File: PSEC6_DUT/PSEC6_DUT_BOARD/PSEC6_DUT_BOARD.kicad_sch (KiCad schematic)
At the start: 0 parts

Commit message: Added Additional Pages for Schematic Distribution
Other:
- added sheet ADC_Buffers (ADC_Buffers.kicad_sch)
- added sheet PLL (PLL.kicad_sch)
- added sheet PSEC6_Device (PSEC6_Device.kicad_sch)
- added sheet SAMTEC (SAMTEC.kicad_sch)
- added sheet SMA (SMA.kicad_sch)
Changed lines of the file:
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@@
 (kicad_sch
-	(version 20250114)
+	(version 20260306)
 	(generator "eeschema")
-	(generator_version "9.0")
-	(paper "A4")
+	(generator_version "10.0")
+	(paper "A3")
+	(sheet
+		(at 25.4 101.6)
+		(size 76.2 50.8)
+		(exclude_from_sim no)
+		(in_bom yes)
+		(on_board yes)
+		(dnp no)
+		(fields_autoplaced yes)
+		(stroke
+			(width 0.1524)
+			(type solid)
+		)
+		(fill
+			(color 0 0 0 0)
+		)
+		(property "Sheetname" "ADC_Buffers"
+			(at 25.4 100.8884 0)
+			(show_name no)
+			(do_not_autoplace no)
+			(effects
+				(font
+					(size 1.27 1.27)
+				)
+				(justify left bottom)
+			)
+		)
+		(property "Sheetfile" "ADC_Buffers.kicad_sch"
+			(at 25.4 152.9846 0)
+			(show_name no)
+			(do_not_autoplace no)
+			(effects
+				(font
+					(size 1.27 1.27)
+				)
+				(justify left top)
+			)
+		)
+		(instances
+			(project "PSEC6_DUT_BOARD"
+				(path "/8c40eb8b-eb69-4f86-94a6-a024d0100f86"
+					(page "3")
+				)
+			)
+		)
+	)
+	(sheet
+		(at 25.4 177.8)
+		(size 76.2 50.8)
+		(exclude_from_sim no)
+		(in_bom yes)
+		(on_board yes)
+		(dnp no)
+		(fields_autoplaced yes)
+		(stroke
+			(width 0.1524)
+			(type solid)
+		)
+		(fill
+			(color 0 0 0 0)
+		)
+		(property "Sheetname" "SMA"
+			(at 25.4 177.0884 0)
+			(show_name no)
+			(do_not_autoplace no)
+			(effects
+				(font
+					(size 1.27 1.27)
+				)
+				(justify left bottom)
+			)
+		)
+		(property "Sheetfile" "SMA.kicad_sch"
+			(at 25.4 229.1846 0)
+			(show_name no)
+			(do_not_autoplace no)
+			(effects
+				(font
+					(size 1.27 1.27)
+				)
+				(justify left top)
+			)
+		)
+		(instances
+			(project "PSEC6_DUT_BOARD"
+				(path "/8c40eb8b-eb69-4f86-94a6-a024d0100f86"
+					(page "4")
+				)
+			)
+		)
+	)
+	(sheet
+		(at 177.8 25.4)
+		(size 76.2 50.8)
+		(exclude_from_sim no)
+		(in_bom yes)
+		(on_board yes)
+		(dnp no)
+		(fields_autoplaced yes)
+		(stroke
+			(width 0.1524)
+			(type solid)
+		)
+		(fill
+			(color 0 0 0 0)
+		)
+		(property "Sheetname" "PLL"
+			(at 177.8 24.6884 0)
+			(show_name no)
+			(do_not_autoplace no)
+			(effects
+				(font
+					(size 1.27 1.27)
+				)
+				(justify left bottom)
+			)
+		)
+		(property "Sheetfile" "PLL.kicad_sch"
+			(at 177.8 76.7846 0)
+			(show_name no)
+			(do_not_autoplace no)
+			(effects
+				(font
+					(size 1.27 1.27)
+				)
+				(justify left top)
+			)
+		)
+		(instances
+			(project "PSEC6_DUT_BOARD"
+				(path "/8c40eb8b-eb69-4f86-94a6-a024d0100f86"
+					(page "5")
+				)
+			)
+		)
+	)
+	(sheet
+		(at 25.4 25.4)
+		(size 76.2 50.8)
+		(exclude_from_sim no)
+		(in_bom yes)
+		(on_board yes)
+		(dnp no)
+		(fields_autoplaced yes)
+		(stroke
+			(width 0.1524)
+			(type solid)
+		)
+		(fill
+			(color 0 0 0 0)
+		)
+		(property "Sheetname" "PSEC6_Device"
+			(at 25.4 24.6884 0)
+			(show_name no)
+			(do_not_autoplace no)
+			(effects
+				(font
+					(size 1.27 1.27)
+				)
+				(justify left bottom)
+			)
+		)
+		(property "Sheetfile" "PSEC6_Device.kicad_sch"
+			(at 25.4 76.7846 0)
+			(show_name no)
+			(do_not_autoplace no)
+			(effects
+				(font
+					(size 1.27 1.27)
+				)
+				(justify left top)
+			)
+		)
+		(instances
+			(project "PSEC6_DUT_BOARD"
+				(path "/8c40eb8b-eb69-4f86-94a6-a024d0100f86"
+					(page "2")
+				)
+			)
+		)
+	)
+	(sheet
+		(at 177.8 101.6)
+		(size 76.2 50.8)
+		(exclude_from_sim no)
+		(in_bom yes)
+		(on_board yes)
+		(dnp no)
+		(fields_autoplaced yes)
+		(stroke
+			(width 0.1524)
+			(type solid)
+		)
+		(fill
+			(color 0 0 0 0)
+		)
+		(property "Sheetname" "SAMTEC"
+			(at 177.8 100.8884 0)
+			(show_name no)
+			(do_not_autoplace no)
+			(effects
+				(font
+					(size 1.27 1.27)
+				)
+				(justify left bottom)
+			)
+		)
+		(property "Sheetfile" "SAMTEC.kicad_sch"
+			(at 177.8 152.9846 0)
+			(show_name no)
+			(do_not_autoplace no)
+			(effects
+				(font
+					(size 1.27 1.27)
+				)
+				(justify left top)
+			)
+		)
+		(instances
+			(project "PSEC6_DUT_BOARD"
+				(path "/8c40eb8b-eb69-4f86-94a6-a024d0100f86"
+					(page "6")
+				)
+			)
+		)
+	)
 	(sheet_instances
 		(path "/"

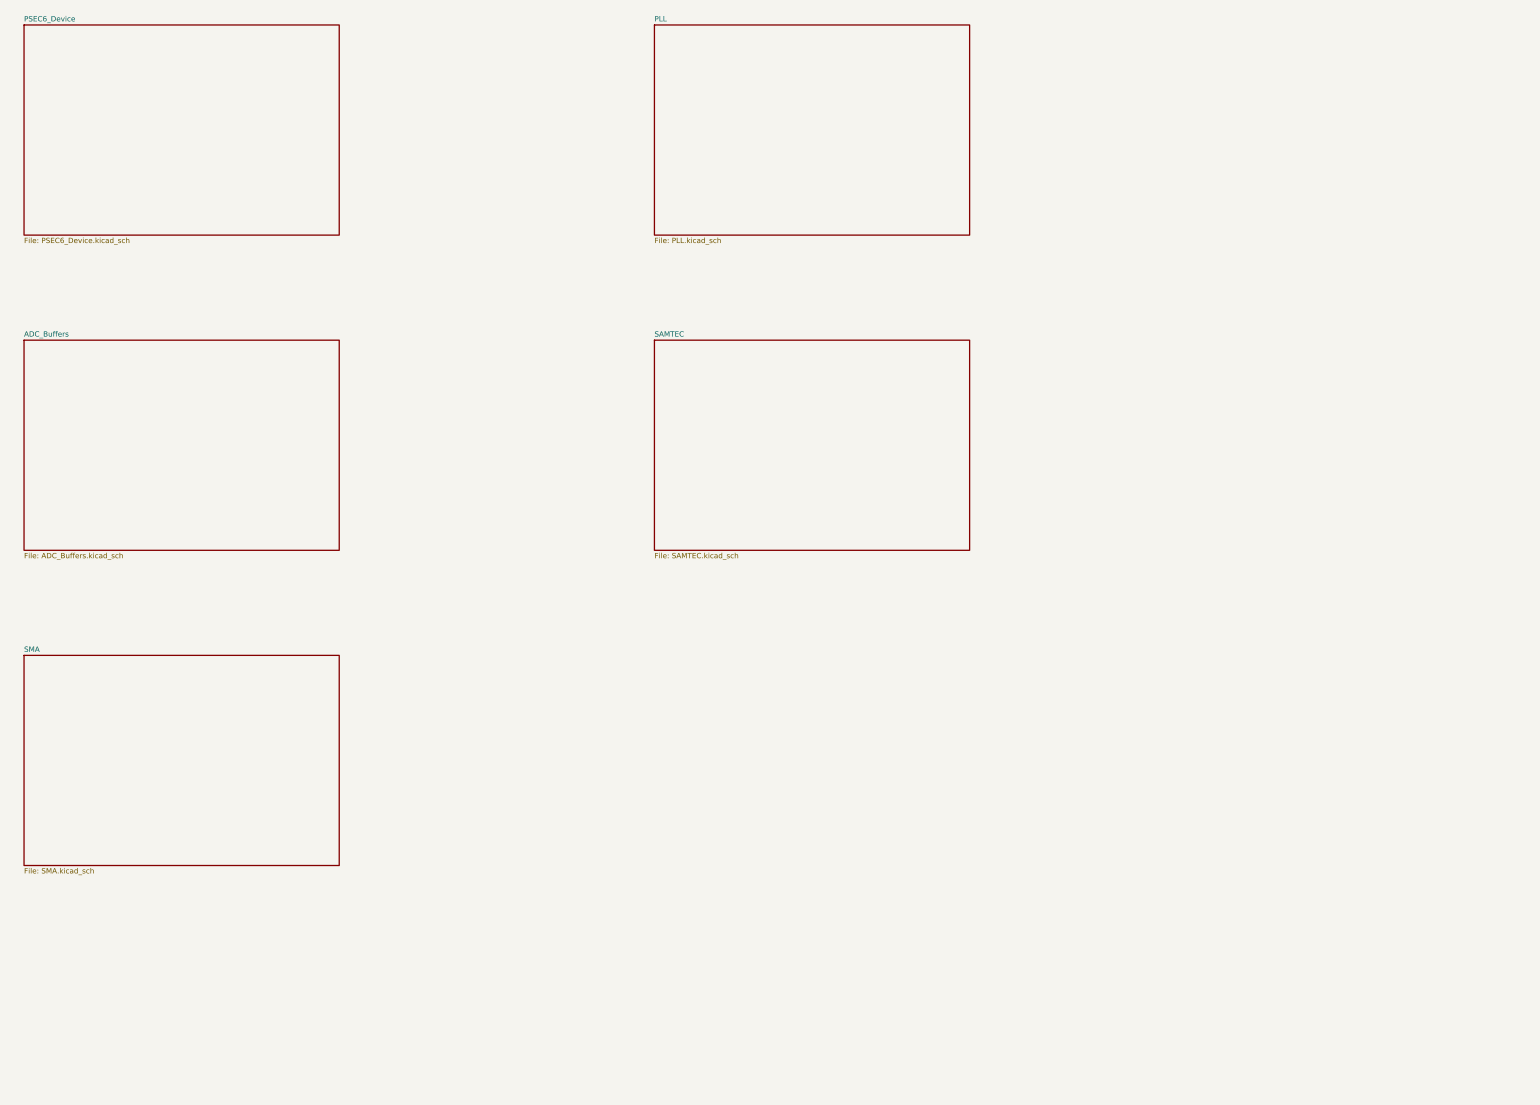
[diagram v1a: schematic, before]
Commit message: created ADC buffer schematic
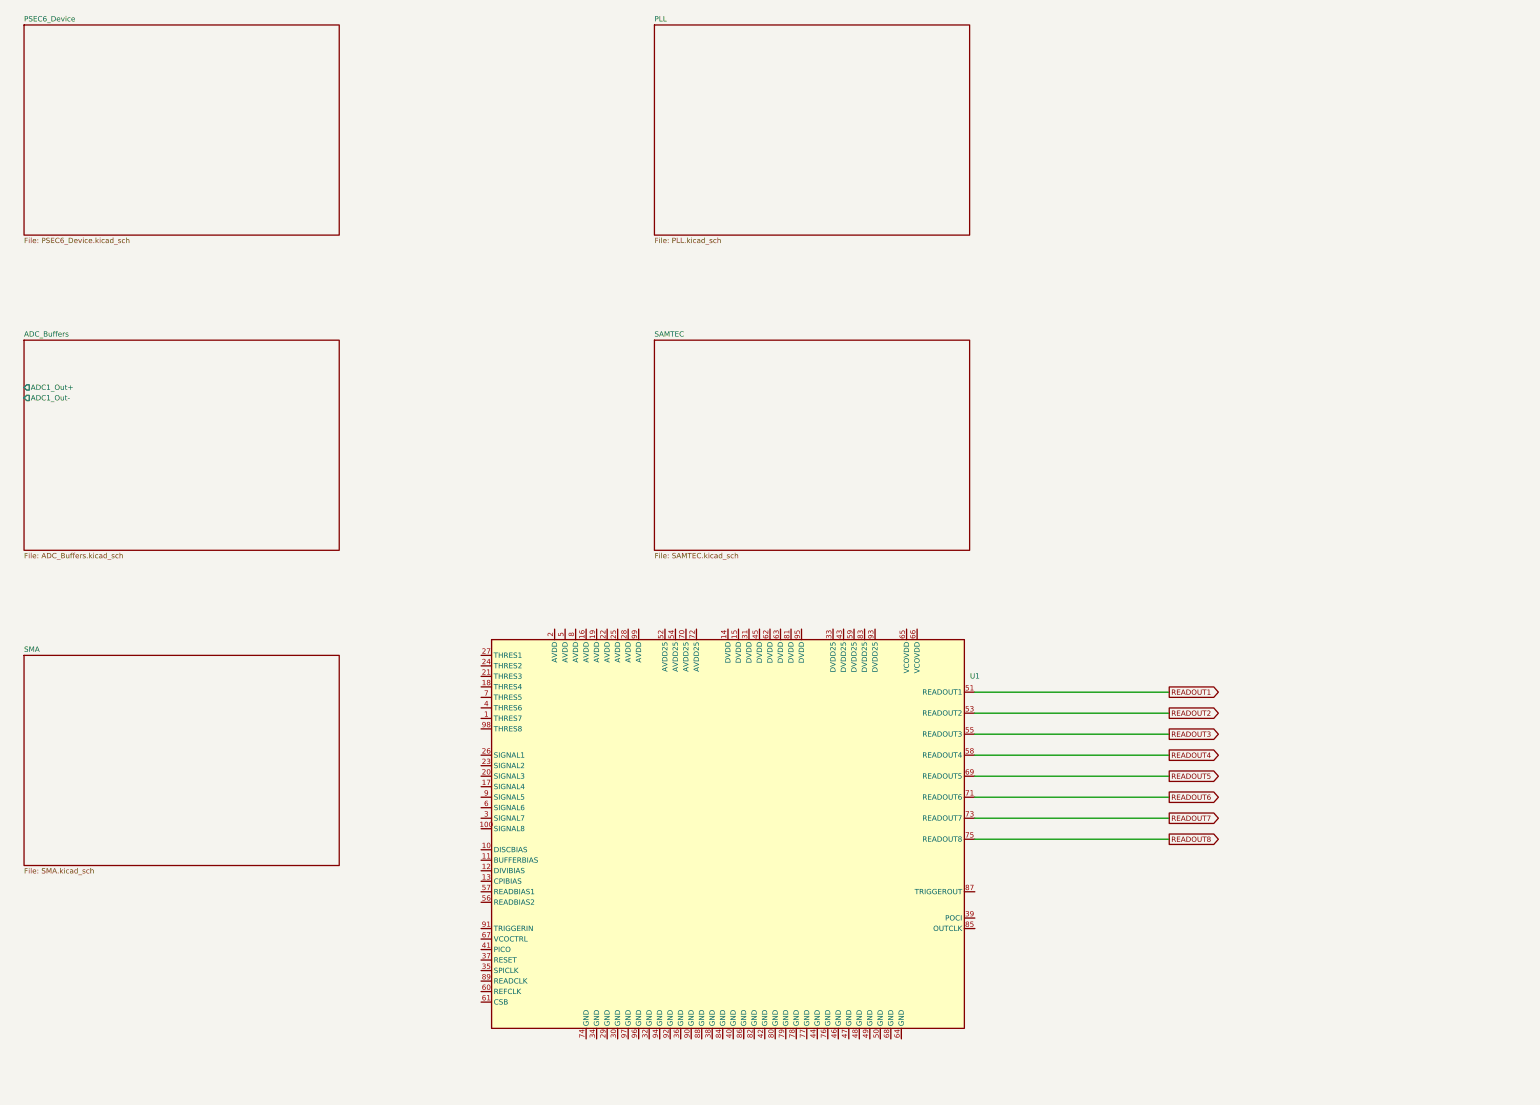
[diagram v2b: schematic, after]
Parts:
- added U1: (no value), symbol PSEC6_Package:PSEC6_Package
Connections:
- new net READOUT1: U1.51 (READOUT1)
- new net READOUT2: U1.53 (READOUT2)
- new net READOUT3: U1.55 (READOUT3)
- new net READOUT4: U1.58 (READOUT4)
- new net READOUT5: U1.69 (READOUT5)
- new net READOUT6: U1.71 (READOUT6)
- new net READOUT7: U1.73 (READOUT7)
- new net READOUT8: U1.75 (READOUT8)
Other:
- sheet ADC_Buffers ports: added ADC1_Out+, ADC1_Out-; removed none

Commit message: Updating values and added RC filters for DUT Card
Added RC filters onto the bias signals and discriminator thresholds, and added RCL values for the SMA devices to provide good DC biasing voltage from the pedestals.
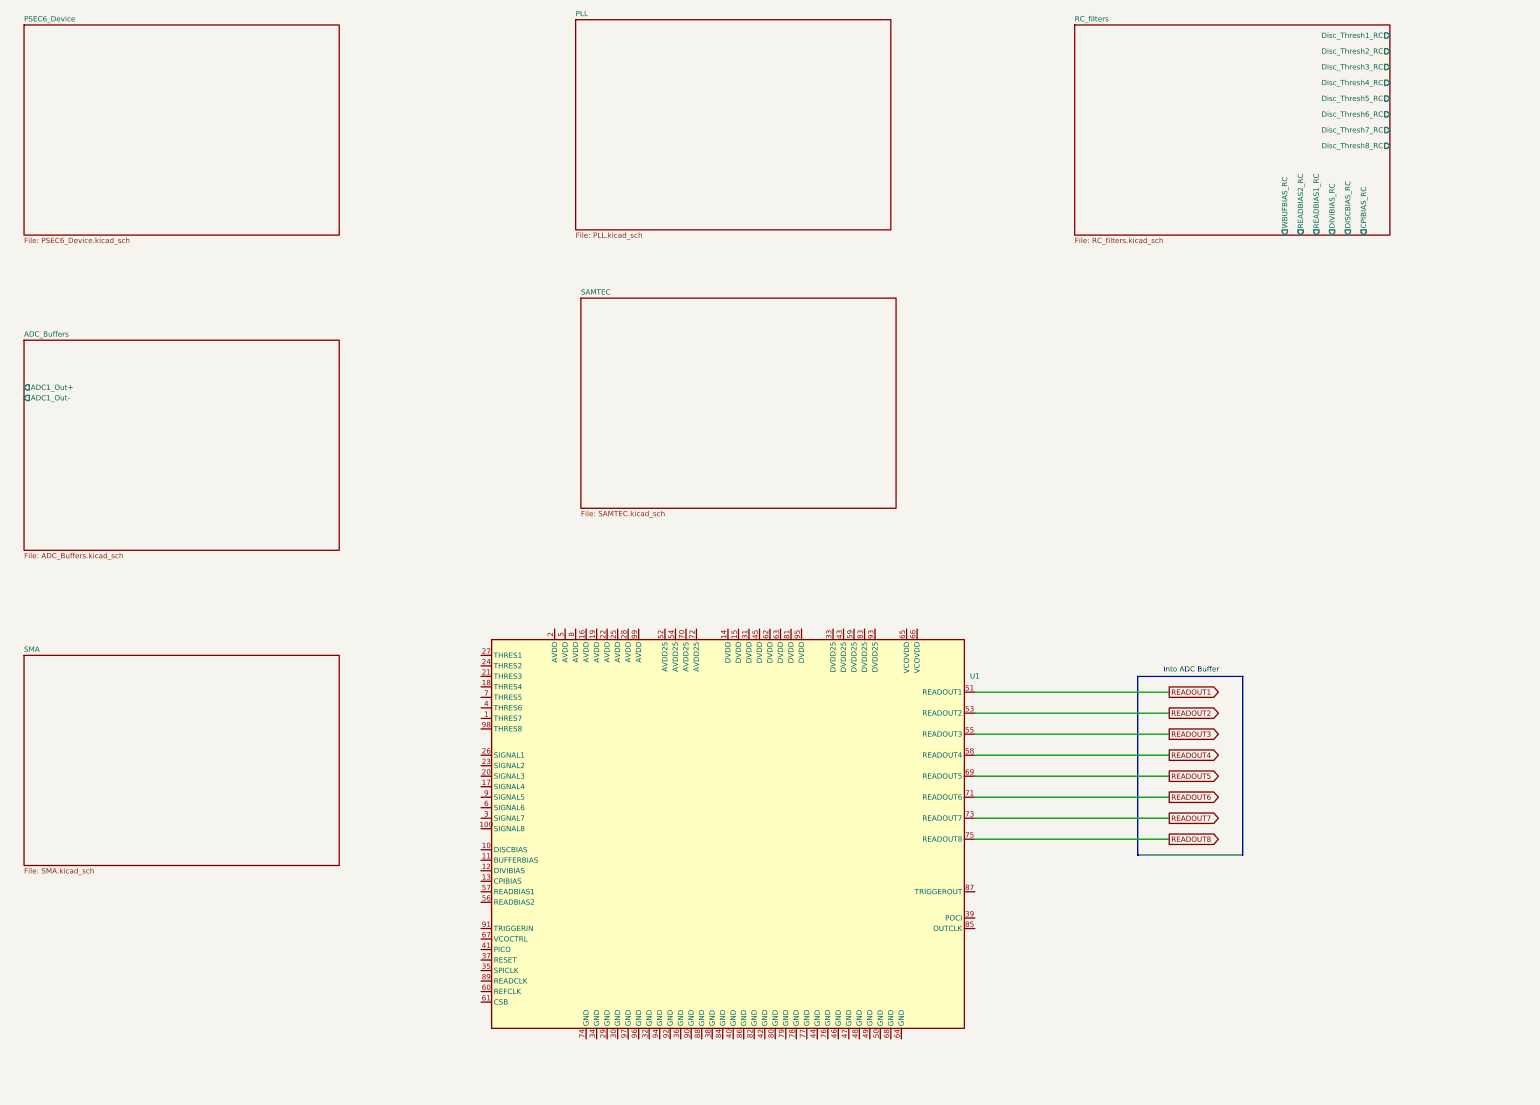
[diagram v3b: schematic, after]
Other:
- added sheet RC_filters (RC_filters.kicad_sch)
- note added: "Into ADC Buffer"
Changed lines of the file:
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@@
 	(generator_version "10.0")
 	(paper "A3")
+	(rectangle
+		(start 294.64 182.88)
+		(end 320.04 226.06)
+		(stroke
+			(width 0)
+			(type default)
+		)
+		(fill
+			(type none)
+		)
+	)
+	(text "Into ADC Buffer"
+		(exclude_from_sim no)
+		(at 307.594 181.356 0)
+		(effects
+			(font
+				(size 1.27 1.27)
+			)
+		)
+	)
 	(wire
 		(pts
@@
 	)
 	(sheet
+		(at 279.4 25.4)
+		(size 76.2 50.8)
+		(exclude_from_sim no)
+		(in_bom yes)
+		(on_board yes)
+		(dnp no)
+		(fields_autoplaced yes)
+		(stroke
+			(width 0.1524)
+			(type solid)
+		)
+		(fill
+			(color 0 0 0 0)
+		)
+		(property "Sheetname" "RC_filters"
+			(at 279.4 24.6884 0)
+			(show_name no)
+			(do_not_autoplace no)
+			(effects
+				(font
+					(size 1.27 1.27)
+				)
+				(justify left bottom)
+			)
+		)
+		(property "Sheetfile" "RC_filters.kicad_sch"
+			(at 279.4 76.7846 0)
+			(show_name no)
+			(do_not_autoplace no)
+			(effects
+				(font
+					(size 1.27 1.27)
+				)
+				(justify left top)
+			)
+		)
+		(pin "Disc_Thresh1_RC" output
+			(at 355.6 27.94 0)
+			(effects
+				(font
+					(size 1.27 1.27)
+				)
+				(justify right)
+			)
+		)
+		(pin "Disc_Thresh2_RC" output
+			(at 355.6 31.75 0)
+			(effects
+				(font
+					(size 1.27 1.27)
+				)
+				(justify right)
+			)
+		)
+		(pin "Disc_Thresh3_RC" output
+			(at 355.6 35.56 0)
+			(effects
+				(font
+					(size 1.27 1.27)
+				)
+				(justify right)
+			)
+		)
+		(pin "Disc_Thresh4_RC" output
+			(at 355.6 39.37 0)
+			(effects
+				(font
+					(size 1.27 1.27)
+				)
+				(justify right)
+			)
+		)
+		(pin "Disc_Thresh5_RC" output
+			(at 355.6 43.18 0)
+			(effects
+				(font
+					(size 1.27 1.27)
+				)
+				(justify right)
+			)
+		)
+		(pin "Disc_Thresh6_RC" output
+			(at 355.6 46.99 0)
+			(effects
+				(font
+					(size 1.27 1.27)
+				)
+				(justify right)
+			)
+		)
+		(pin "Disc_Thresh7_RC" output
+			(at 355.6 50.8 0)
+			(effects
+				(font
+					(size 1.27 1.27)
+				)
+				(justify right)
+			)
+		)
+		(pin "Disc_Thresh8_RC" output
+			(at 355.6 54.61 0)
+			(effects
+				(font
+					(size 1.27 1.27)
+				)
+				(justify right)
+			)
+		)
+		(pin "CPIBIAS_RC" output
+			(at 349.25 76.2 270)
+			(effects
+				(font
+					(size 1.27 1.27)
+				)
+				(justify left)
+			)
+		)
+		(pin "DISCBIAS_RC" output
+			(at 345.44 76.2 270)
+			(effects
+				(font
+					(size 1.27 1.27)
+				)
+				(justify left)
+			)
+		)
+		(pin "DIVIBIAS_RC" output
+			(at 341.63 76.2 270)
+			(effects
+				(font
+					(size 1.27 1.27)
+				)
+				(justify left)
+			)
+		)
+		(pin "READBIAS1_RC" output
+			(at 337.82 76.2 270)
+			(effects
+				(font
+					(size 1.27 1.27)
+				)
+				(justify left)
+			)
+		)
+		(pin "READBIAS2_RC" output
+			(at 334.01 76.2 270)
+			(effects
+				(font
+					(size 1.27 1.27)
+				)
+				(justify left)
+			)
+		)
+		(pin "WBUFBIAS_RC" output
+			(at 330.2 76.2 270)
+			(effects
+				(font
+					(size 1.27 1.27)
+				)
+				(justify left)
+			)
+		)
+		(instances
+			(project "PSEC6_DUT_BOARD"
+				(path "/8c40eb8b-eb69-4f86-94a6-a024d0100f86"
+					(page "7")
+				)
+			)
+		)
+	)
+	(sheet
 		(at 25.4 101.6)
 		(size 76.2 50.8)
@@
 	)
 	(sheet
-		(at 177.8 25.4)
+		(at 158.75 24.13)
 		(size 76.2 50.8)
 		(exclude_from_sim no)
@@
 		)
 		(property "Sheetname" "PLL"
-			(at 177.8 24.6884 0)
+			(at 158.75 23.4184 0)
 			(show_name no)
 			(do_not_autoplace no)
@@
 		)
 		(property "Sheetfile" "PLL.kicad_sch"
-			(at 177.8 76.7846 0)
+			(at 158.75 75.5146 0)
 			(show_name no)
 			(do_not_autoplace no)
@@
 	)
 	(sheet
-		(at 177.8 101.6)
+		(at 160.02 91.44)
 		(size 76.2 50.8)
 		(exclude_from_sim no)
@@
 		)
 		(property "Sheetname" "SAMTEC"
-			(at 177.8 100.8884 0)
+			(at 160.02 90.7284 0)
 			(show_name no)
 			(do_not_autoplace no)
@@
 		)
 		(property "Sheetfile" "SAMTEC.kicad_sch"
-			(at 177.8 152.9846 0)
-			(show_name no)
-			(do_not_autoplace no)
+			(at 160.02 142.8246 0)
+			(show_name no)
+			(do_not_autoplace no)
